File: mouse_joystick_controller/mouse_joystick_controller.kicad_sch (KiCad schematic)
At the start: 0 parts

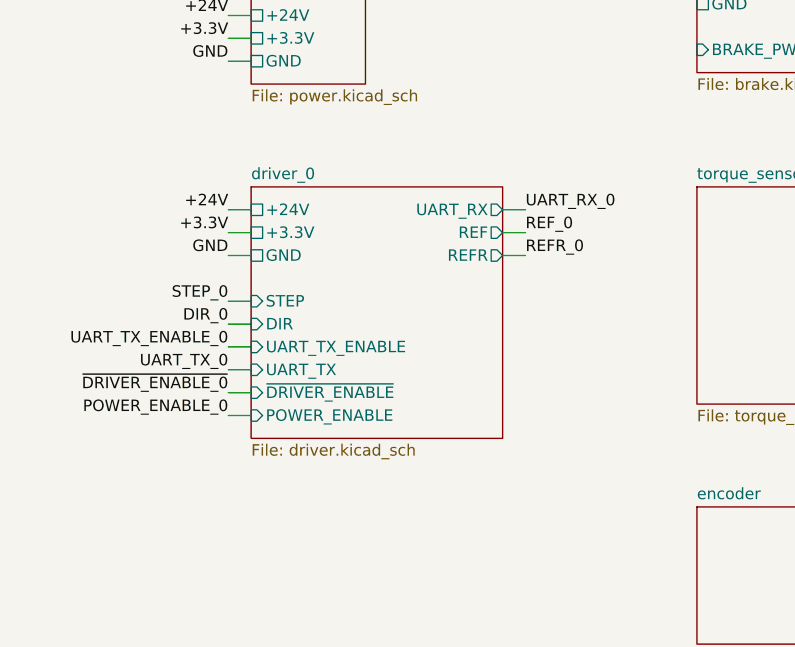
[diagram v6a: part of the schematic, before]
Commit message: Rearrange sheets
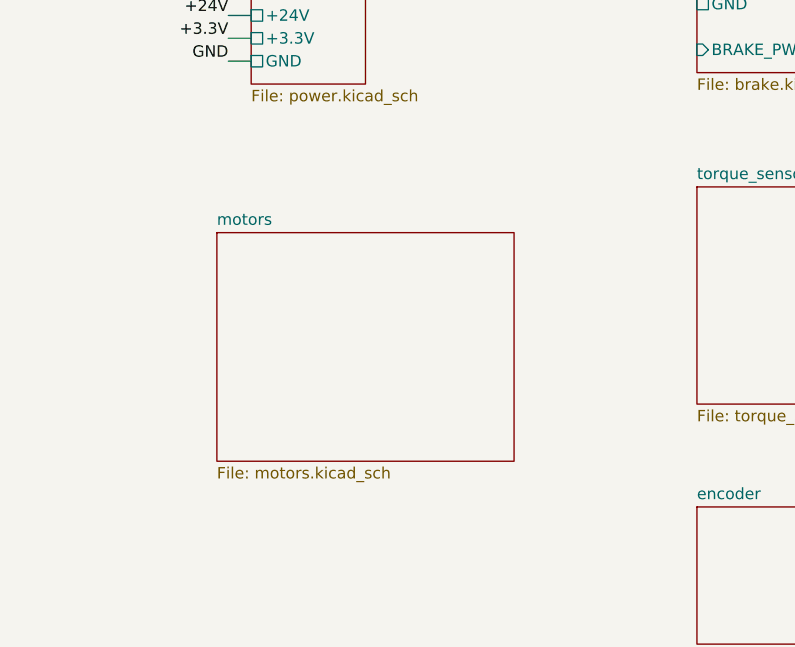
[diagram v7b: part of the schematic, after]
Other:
- removed sheet driver_0
- added sheet motors (motors.kicad_sch)
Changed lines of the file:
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@@
   (title_block
     (title "mouse_joystick_controller")
-    (date "2023-05-22")
+    (date "2023-05-24")
     (rev "2.0")
     (company "Howard Hughes Medical Institute")
-  )
-  (wire (pts (xy 133.35 105.41) (xy 130.81 105.41))
-    (stroke (width 0) (type default))
-  )
-  (wire (pts (xy 161.29 85.09) (xy 163.83 85.09))
-    (stroke (width 0) (type default))
   )
   (wire (pts (xy 133.35 66.04) (xy 130.81 66.04))
@@
   )
   (wire (pts (xy 133.35 68.58) (xy 130.81 68.58))
-    (stroke (width 0) (type default))
-  )
-  (wire (pts (xy 133.35 87.63) (xy 130.81 87.63))
-    (stroke (width 0) (type default))
-  )
-  (wire (pts (xy 133.35 102.87) (xy 130.81 102.87))
-    (stroke (width 0) (type default))
-  )
-  (wire (pts (xy 133.35 100.33) (xy 130.81 100.33))
-    (stroke (width 0) (type default))
-  )
-  (wire (pts (xy 133.35 85.09) (xy 130.81 85.09))
-    (stroke (width 0) (type default))
-  )
-  (wire (pts (xy 161.29 90.17) (xy 163.83 90.17))
-    (stroke (width 0) (type default))
-  )
-  (wire (pts (xy 133.35 107.95) (xy 130.81 107.95))
-    (stroke (width 0) (type default))
-  )
-  (wire (pts (xy 133.35 95.25) (xy 130.81 95.25))
     (stroke (width 0) (type default))
   )
@@
     (stroke (width 0) (type default))
   )
-  (wire (pts (xy 133.35 90.17) (xy 130.81 90.17))
-    (stroke (width 0) (type default))
-  )
-  (wire (pts (xy 133.35 97.79) (xy 130.81 97.79))
-    (stroke (width 0) (type default))
-  )
-  (wire (pts (xy 161.29 87.63) (xy 163.83 87.63))
-    (stroke (width 0) (type default))
-  )
-  (label "GND" (at 130.81 90.17 180) (fields_autoplaced)
-    (effects (font (size 1.27 1.27)) (justify right bottom))
-  )
   (label "+24V" (at 130.81 63.5 180) (fields_autoplaced)
-    (effects (font (size 1.27 1.27)) (justify right bottom))
-  )
-  (label "DIR_0" (at 130.81 97.79 180) (fields_autoplaced)
     (effects (font (size 1.27 1.27)) (justify right bottom))
   )
@@
     (effects (font (size 1.27 1.27)) (justify right bottom))
   )
-  (label "UART_RX_0" (at 163.83 85.09 0) (fields_autoplaced)
-    (effects (font (size 1.27 1.27)) (justify left bottom))
-  )
-  (label "REF_0" (at 163.83 87.63 0) (fields_autoplaced)
-    (effects (font (size 1.27 1.27)) (justify left bottom))
-  )
   (label "GND" (at 130.81 50.8 180) (fields_autoplaced)
     (effects (font (size 1.27 1.27)) (justify right bottom))
   )
   (label "+3.3V" (at 130.81 66.04 180) (fields_autoplaced)
-    (effects (font (size 1.27 1.27)) (justify right bottom))
-  )
-  (label "~{DRIVER_ENABLE_0}" (at 130.81 105.41 180) (fields_autoplaced)
-    (effects (font (size 1.27 1.27)) (justify right bottom))
-  )
-  (label "STEP_0" (at 130.81 95.25 180) (fields_autoplaced)
-    (effects (font (size 1.27 1.27)) (justify right bottom))
-  )
-  (label "POWER_ENABLE_0" (at 130.81 107.95 180) (fields_autoplaced)
-    (effects (font (size 1.27 1.27)) (justify right bottom))
-  )
-  (label "UART_TX_ENABLE_0" (at 130.81 100.33 180) (fields_autoplaced)
-    (effects (font (size 1.27 1.27)) (justify right bottom))
-  )
-  (label "REFR_0" (at 163.83 90.17 0) (fields_autoplaced)
-    (effects (font (size 1.27 1.27)) (justify left bottom))
-  )
-  (label "UART_TX_0" (at 130.81 102.87 180) (fields_autoplaced)
-    (effects (font (size 1.27 1.27)) (justify right bottom))
-  )
-  (label "+24V" (at 130.81 85.09 180) (fields_autoplaced)
-    (effects (font (size 1.27 1.27)) (justify right bottom))
-  )
-  (label "+3.3V" (at 130.81 87.63 180) (fields_autoplaced)
     (effects (font (size 1.27 1.27)) (justify right bottom))
   )
@@
     )
   )
+  (sheet (at 129.54 87.63) (size 33.02 25.4) (fields_autoplaced)
+    (stroke (width 0.1524) (type solid))
+    (fill (color 0 0 0 0.0000))
+    (property "Sheetname" "motors" (at 129.54 86.9184 0)
+      (effects (font (size 1.27 1.27)) (justify left bottom))
+    )
+    (property "Sheetfile" "motors.kicad_sch" (at 129.54 113.6146 0)
+      (effects (font (size 1.27 1.27)) (justify left top))
+    )
+    (instances
+      (project "mouse_joystick_controller"
+        (path "/cc457ebc-4af6-4663-b19f-8cb38f061cb4" (page "11"))
+      )
+    )
+  )
   (sheet (at 182.88 57.15) (size 22.86 12.7) (fields_autoplaced)
     (stroke (width 0.1524) (type solid))
@@
       )
     )
-  )
-  (sheet (at 133.35 82.55) (size 27.94 27.94) (fields_autoplaced)
-    (stroke (width 0.1524) (type solid))
-    (fill (color 0 0 0 0.0000))
-    (property "Sheetname" "driver_0" (at 133.35 81.8384 0)
-      (effects (font (size 1.27 1.27)) (justify left bottom))
-    )
-    (property "Sheetfile" "driver.kicad_sch" (at 133.35 111.0746 0)
-      (effects (font (size 1.27 1.27)) (justify left top))
-    )
-    (pin "POWER_ENABLE" input (at 133.35 107.95 180)
-      (effects (font (size 1.27 1.27)) (justify left))
-    )
-    (pin "~{DRIVER_ENABLE}" input (at 133.35 105.41 180)
-      (effects (font (size 1.27 1.27)) (justify left))
-    )
-    (pin "REFR" output (at 161.29 90.17 0)
-      (effects (font (size 1.27 1.27)) (justify right))
-    )
-    (pin "REF" output (at 161.29 87.63 0)
-      (effects (font (size 1.27 1.27)) (justify right))
-    )
-    (pin "UART_RX" output (at 161.29 85.09 0)
-      (effects (font (size 1.27 1.27)) (justify right))
-    )
-    (pin "UART_TX" input (at 133.35 102.87 180)
-      (effects (font (size 1.27 1.27)) (justify left))
-    )
-    (pin "UART_TX_ENABLE" input (at 133.35 100.33 180)
-      (effects (font (size 1.27 1.27)) (justify left))
-    )
-    (pin "GND" passive (at 133.35 90.17 180)
-      (effects (font (size 1.27 1.27)) (justify left))
-    )
-    (pin "STEP" input (at 133.35 95.25 180)
-      (effects (font (size 1.27 1.27)) (justify left))
-    )
-    (pin "DIR" input (at 133.35 97.79 180)
-      (effects (font (size 1.27 1.27)) (justify left))
-    )
-    (pin "+3.3V" passive (at 133.35 87.63 180)
-      (effects (font (size 1.27 1.27)) (justify left))
-    )
-    (pin "+24V" passive (at 133.35 85.09 180)
-      (effects (font (size 1.27 1.27)) (justify left))
-    )
-    (instances
-      (project "mouse_joystick_controller"
-        (path "/cc457ebc-4af6-4663-b19f-8cb38f061cb4" (page "3"))
-      )
-    )

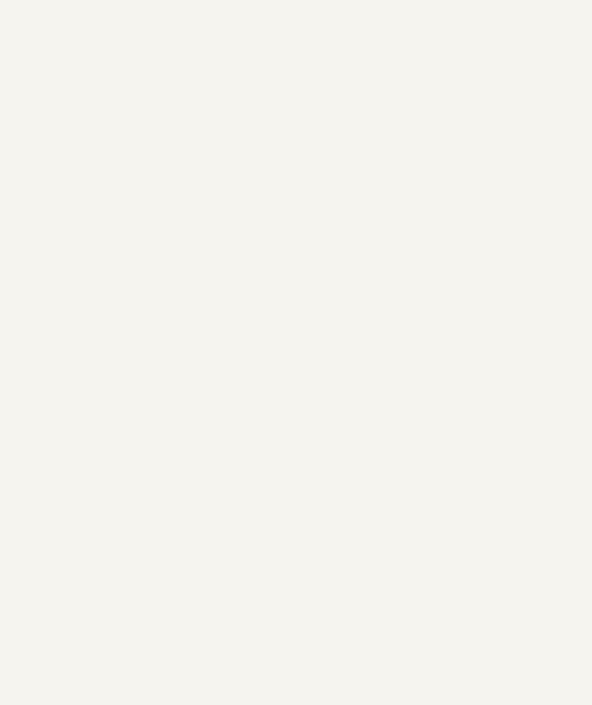
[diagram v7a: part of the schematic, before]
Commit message: Add microcontroller sheet
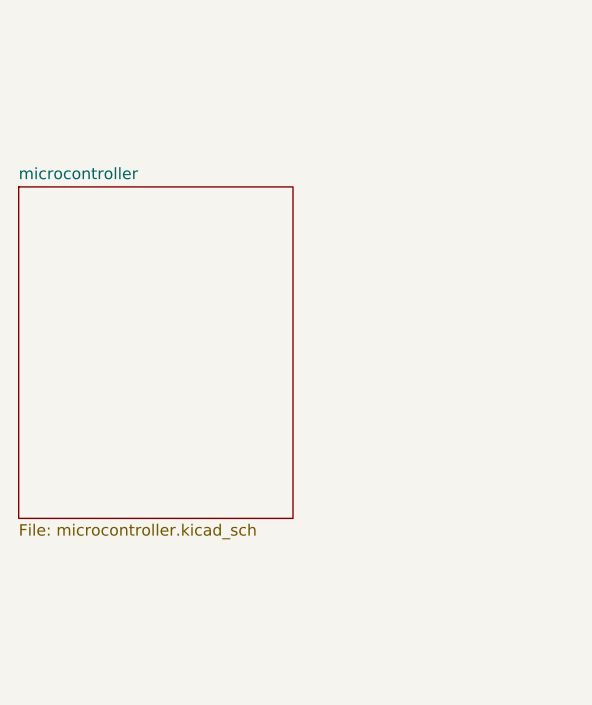
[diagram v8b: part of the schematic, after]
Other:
- added sheet microcontroller (microcontroller.kicad_sch)
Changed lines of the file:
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@@
+    )
+  )
+  (sheet (at 52.07 64.77) (size 30.48 36.83) (fields_autoplaced)
+    (stroke (width 0.1524) (type solid))
+    (fill (color 0 0 0 0.0000))
+    (property "Sheetname" "microcontroller" (at 52.07 64.0584 0)
+      (effects (font (size 1.27 1.27)) (justify left bottom))
+    )
+    (property "Sheetfile" "microcontroller.kicad_sch" (at 52.07 102.1846 0)
+      (effects (font (size 1.27 1.27)) (justify left top))
+    )
+    (property "Field2" "" (at 52.07 64.77 0)
+      (effects (font (size 1.27 1.27)) hide)
+    )
+    (instances
+      (project "mouse_joystick_controller"
+        (path "/cc457ebc-4af6-4663-b19f-8cb38f061cb4" (page "12"))
+      )
     )
   )
